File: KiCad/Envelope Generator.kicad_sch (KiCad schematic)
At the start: 36 parts, among them U7 TL074, U8 TL074

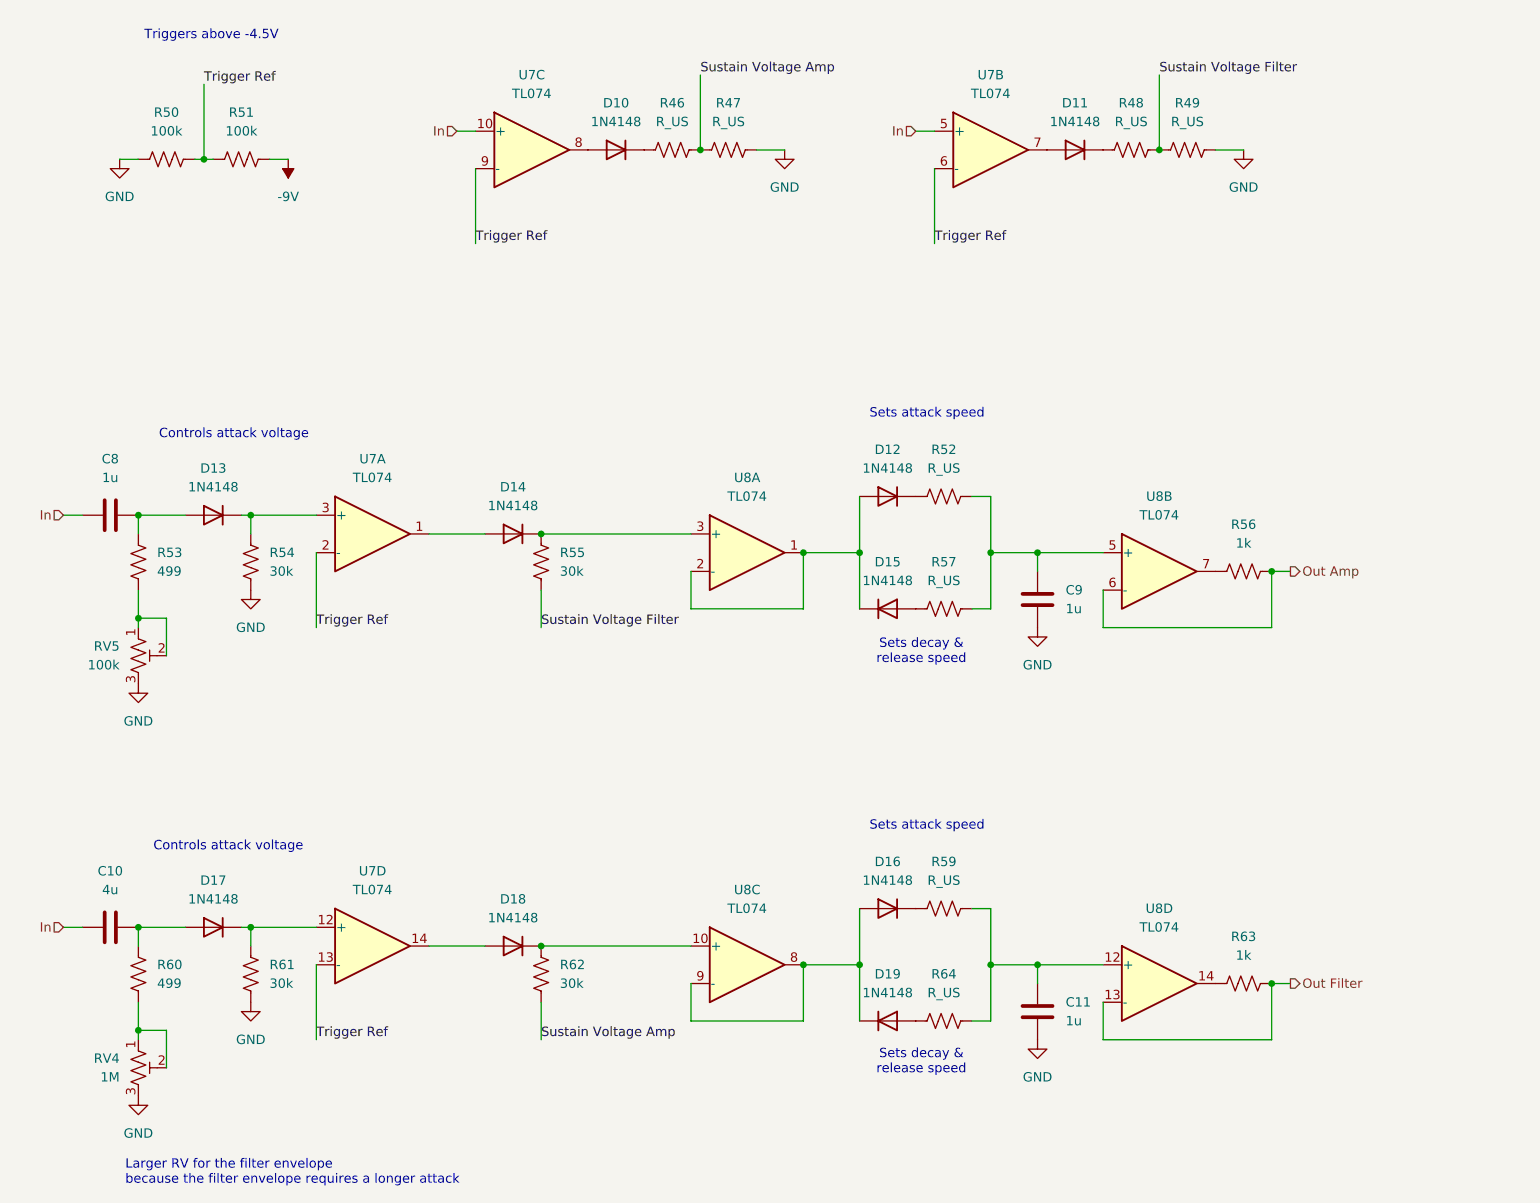
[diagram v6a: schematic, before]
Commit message: added potentiometer voltage control cct
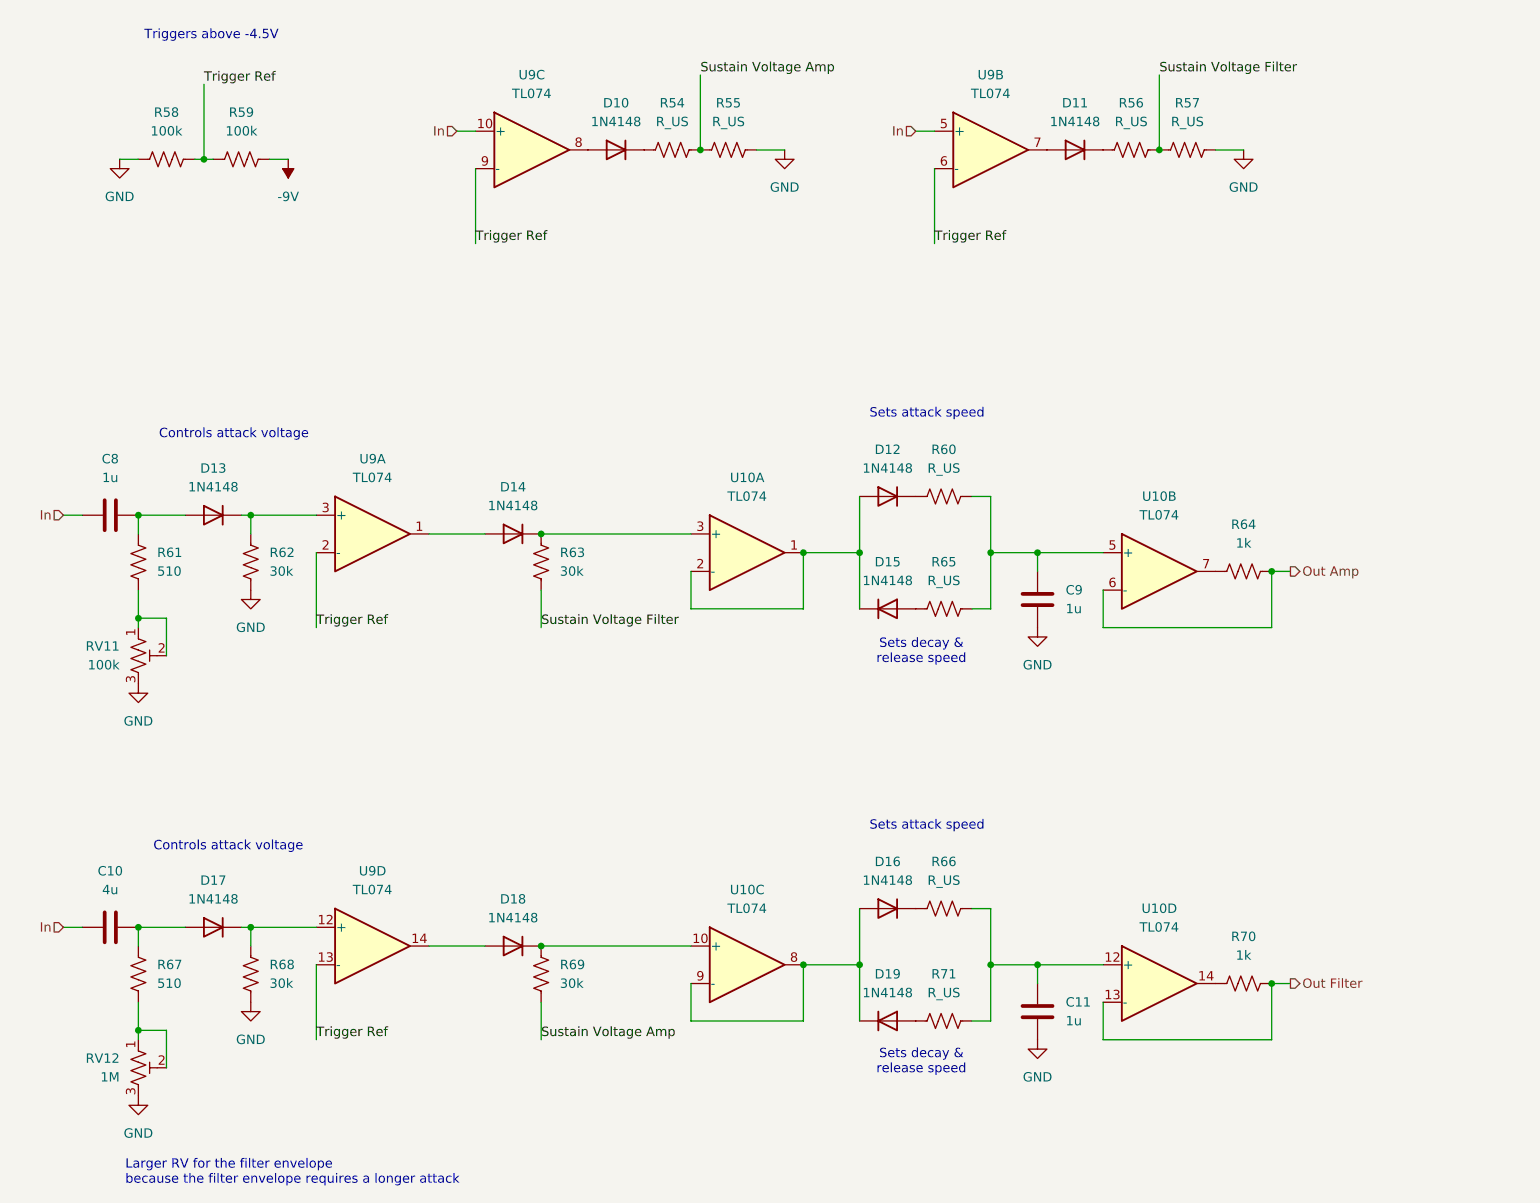
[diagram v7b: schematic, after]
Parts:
- R61: renamed from R53; value 499 -> 510; footprint Resistor_THT:R_Axial_DIN0207_L6.3mm_D2.5mm_P7.62mm_Horizontal -> Resistor_SMD:R_0201_0603Metric
- R67: renamed from R60; value 499 -> 510; footprint Resistor_THT:R_Axial_DIN0207_L6.3mm_D2.5mm_P7.62mm_Horizontal -> Resistor_SMD:R_0201_0603Metric
- renumbered R46 to R54, R47 to R55, R48 to R56, R49 to R57, R50 to R58, R51 to R59, R52 to R60, R54 to R62, R55 to R63, R56 to R64, R57 to R65, R59 to R66, R61 to R68, R62 to R69, R63 to R70, R64 to R71, RV5 to RV11, RV4 to RV12, U8 to U10, U7 to U9

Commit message: added volume control knob
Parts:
- renumbered RV11 to RV12, RV12 to RV13
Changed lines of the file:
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@@
 		(dnp no)
 		(fields_autoplaced yes)
-		(property "Reference" "#PWR073"
+		(property "Reference" "#PWR074"
 			(at 49.53 162.56 0)
 			(hide yes)
@@
 			(project "Electronic Trombone"
 				(path "/931827f3-33b7-460f-8885-7db258da2648/77fe3443-32fb-46cd-8502-6f8d1ae6ff63"
-					(reference "#PWR073")
+					(reference "#PWR074")
 					(unit 1)
 				)
@@
 		(dnp no)
 		(fields_autoplaced yes)
-		(property "Reference" "#PWR067"
+		(property "Reference" "#PWR068"
 			(at 184.15 46.99 0)
 			(hide yes)
@@
 			(project "Electronic Trombone"
 				(path "/931827f3-33b7-460f-8885-7db258da2648/77fe3443-32fb-46cd-8502-6f8d1ae6ff63"
-					(reference "#PWR067")
+					(reference "#PWR068")
 					(unit 1)
 				)
@@
 		(dnp no)
 		(fields_autoplaced yes)
-		(property "Reference" "#PWR068"
+		(property "Reference" "#PWR069"
 			(at 31.75 48.26 0)
 			(hide yes)
@@
 			(project "Electronic Trombone"
 				(path "/931827f3-33b7-460f-8885-7db258da2648/77fe3443-32fb-46cd-8502-6f8d1ae6ff63"
-					(reference "#PWR068")
+					(reference "#PWR069")
 					(unit 1)
 				)
@@
 		(dnp no)
 		(fields_autoplaced yes)
-		(property "Reference" "RV11"
+		(property "Reference" "RV12"
 			(at 31.75 107.9499 0)
 			(show_name no)
@@
 			(project "Electronic Trombone"
 				(path "/931827f3-33b7-460f-8885-7db258da2648/77fe3443-32fb-46cd-8502-6f8d1ae6ff63"
-					(reference "RV11")
+					(reference "RV12")
 					(unit 1)
 				)
@@
 		(dnp no)
 		(fields_autoplaced yes)
-		(property "Reference" "#PWR069"
+		(property "Reference" "#PWR070"
 			(at 54.61 38.1 0)
 			(hide yes)
@@
 			(project "Electronic Trombone"
 				(path "/931827f3-33b7-460f-8885-7db258da2648/77fe3443-32fb-46cd-8502-6f8d1ae6ff63"
-					(reference "#PWR069")
+					(reference "#PWR070")
 					(unit 1)
 				)
@@
 		(dnp no)
 		(fields_autoplaced yes)
-		(property "Reference" "#PWR066"
+		(property "Reference" "#PWR067"
 			(at 121.92 46.99 0)
 			(hide yes)
@@
 			(project "Electronic Trombone"
 				(path "/931827f3-33b7-460f-8885-7db258da2648/77fe3443-32fb-46cd-8502-6f8d1ae6ff63"
-					(reference "#PWR066")
+					(reference "#PWR067")
 					(unit 1)
 				)
@@
 		(dnp no)
 		(fields_autoplaced yes)
-		(property "Reference" "#PWR075"
+		(property "Reference" "#PWR076"
 			(at 34.29 175.26 0)
 			(hide yes)
@@
 			(project "Electronic Trombone"
 				(path "/931827f3-33b7-460f-8885-7db258da2648/77fe3443-32fb-46cd-8502-6f8d1ae6ff63"
-					(reference "#PWR075")
+					(reference "#PWR076")
 					(unit 1)
 				)
@@
 		(dnp no)
 		(fields_autoplaced yes)
-		(property "Reference" "#PWR072"
+		(property "Reference" "#PWR073"
 			(at 34.29 119.38 0)
 			(hide yes)
@@
 			(project "Electronic Trombone"
 				(path "/931827f3-33b7-460f-8885-7db258da2648/77fe3443-32fb-46cd-8502-6f8d1ae6ff63"
-					(reference "#PWR072")
+					(reference "#PWR073")
 					(unit 1)
 				)
@@
 		(dnp no)
 		(fields_autoplaced yes)
-		(property "Reference" "#PWR074"
+		(property "Reference" "#PWR075"
 			(at 156.21 167.64 0)
 			(hide yes)
@@
 			(project "Electronic Trombone"
 				(path "/931827f3-33b7-460f-8885-7db258da2648/77fe3443-32fb-46cd-8502-6f8d1ae6ff63"
-					(reference "#PWR074")
+					(reference "#PWR075")
 					(unit 1)
 				)
@@
 		(dnp no)
 		(fields_autoplaced yes)
-		(property "Reference" "#PWR070"
+		(property "Reference" "#PWR071"
 			(at 49.53 106.68 0)
 			(hide yes)
@@
 			(project "Electronic Trombone"
 				(path "/931827f3-33b7-460f-8885-7db258da2648/77fe3443-32fb-46cd-8502-6f8d1ae6ff63"
-					(reference "#PWR070")
+					(reference "#PWR071")
 					(unit 1)
 				)
@@
 		(dnp no)
 		(fields_autoplaced yes)
-		(property "Reference" "RV12"
+		(property "Reference" "RV13"
 			(at 31.75 163.8299 0)
 			(show_name no)
@@
 			(project "Electronic Trombone"
 				(path "/931827f3-33b7-460f-8885-7db258da2648/77fe3443-32fb-46cd-8502-6f8d1ae6ff63"
-					(reference "RV12")
+					(reference "RV13")
 					(unit 1)
 				)
@@
 		(dnp no)
 		(fields_autoplaced yes)
-		(property "Reference" "#PWR071"
+		(property "Reference" "#PWR072"
 			(at 156.21 111.76 0)
 			(hide yes)
@@
 			(project "Electronic Trombone"
 				(path "/931827f3-33b7-460f-8885-7db258da2648/77fe3443-32fb-46cd-8502-6f8d1ae6ff63"
-					(reference "#PWR071")
+					(reference "#PWR072")
 					(unit 1)
 				)
